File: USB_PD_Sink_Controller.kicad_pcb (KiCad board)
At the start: 2 copper layers, 43.5 x 30.5 mm, 24 parts, among them J1 USB_C_Receptacle_PowerOnly_6P, J2 Barrel_Jack, J3 Conn_01x15_Socket, J4 Conn_01x15_Socket, U1 STUSB4500QTR, U2 STL6P3LLH6, U3 STL6P3LLH6, U4 LM2931-5.0_SO8

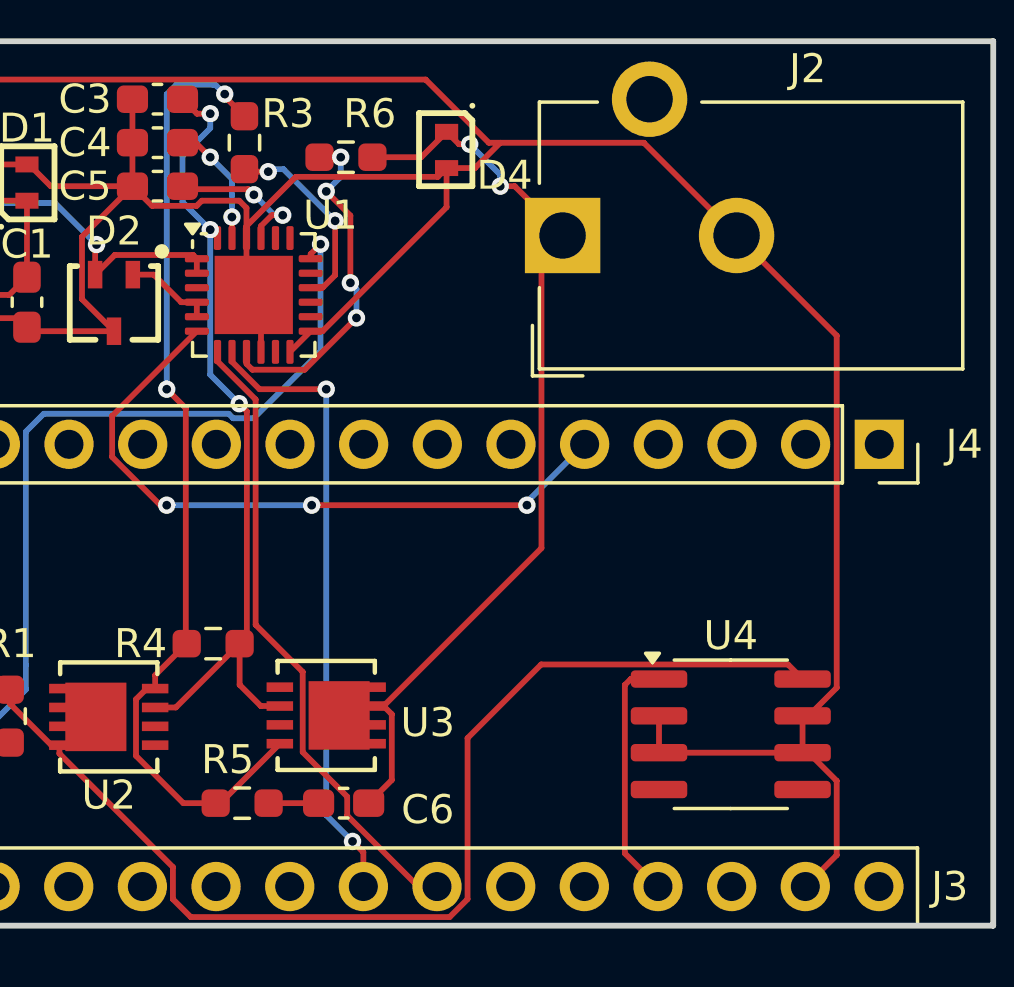
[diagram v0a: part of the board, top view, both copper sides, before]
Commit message: Added Pullup resistors and alert pin
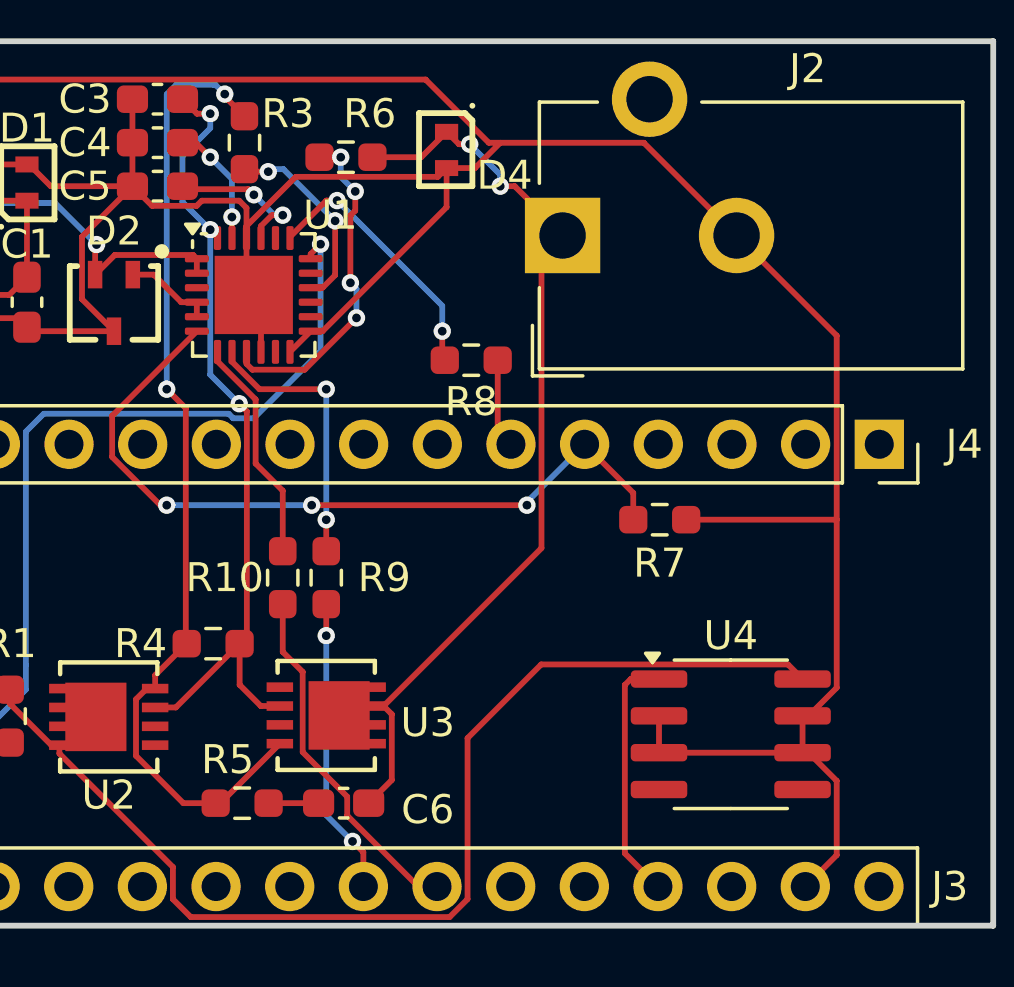
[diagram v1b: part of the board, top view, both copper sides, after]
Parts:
- added R10: 4.7kR, Resistor_SMD:R_0603_1608Metric_Pad0.98x0.95mm_HandSolder, F.Cu at (157.5, 95.5)
- added R7: 10kR, Resistor_SMD:R_0603_1608Metric_Pad0.98x0.95mm_HandSolder, F.Cu at (170.5, 93.5)
- added R8: 4.7kR, Resistor_SMD:R_0603_1608Metric_Pad0.98x0.95mm_HandSolder, F.Cu at (164.0, 88.0)
- added R9: 4.7kR, Resistor_SMD:R_0603_1608Metric_Pad0.98x0.95mm_HandSolder, F.Cu at (159.0, 95.5)
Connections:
- J4 pad 6: unconnected-(J4-Pin_6-Pad6) -> Net-(A1-D3)
- U1 pad 19: unconnected-(U1-ALERT-Pad19) -> Net-(U1-ALERT)
- U1 pad 7: Net-(A1-A5) -> Net-(U1-SCL)
- U1 pad 8: Net-(A1-A4) -> Net-(U1-SDA)
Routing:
- net Net-(A1-A4): track 21.7 -> 10.3 mm
- net Net-(A1-A5): track 22.0 -> 12.3 mm
- net Net-(U1-SDA): track 0.00 -> 9.57 mm, vias 0 -> 2
- net Net-(U1-ALERT): track 0.00 -> 9.22 mm, vias 0 -> 2
- net Net-(U1-SCL): track 0.00 -> 7.81 mm
- net GND: track 139.6 -> 144.8 mm
- net Net-(A1-D2): track 23.5 -> 26.8 mm
- net Net-(A1-D3): track 0.00 -> 3.09 mm

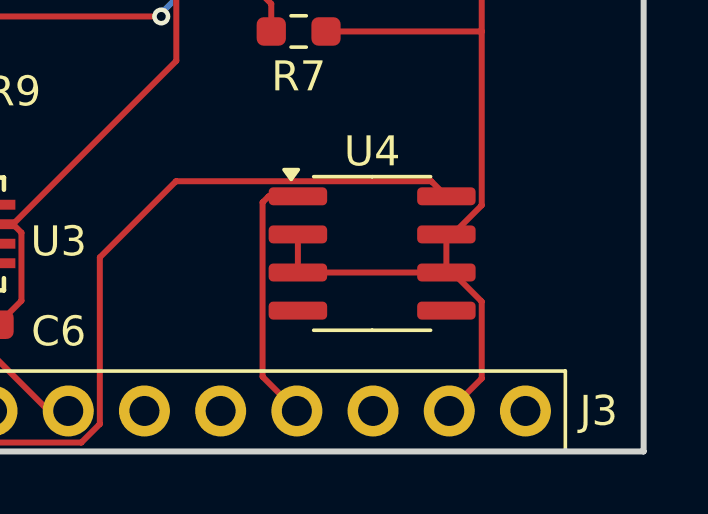
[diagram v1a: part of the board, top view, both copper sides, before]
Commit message: Added capacitor to linear voltage regulator
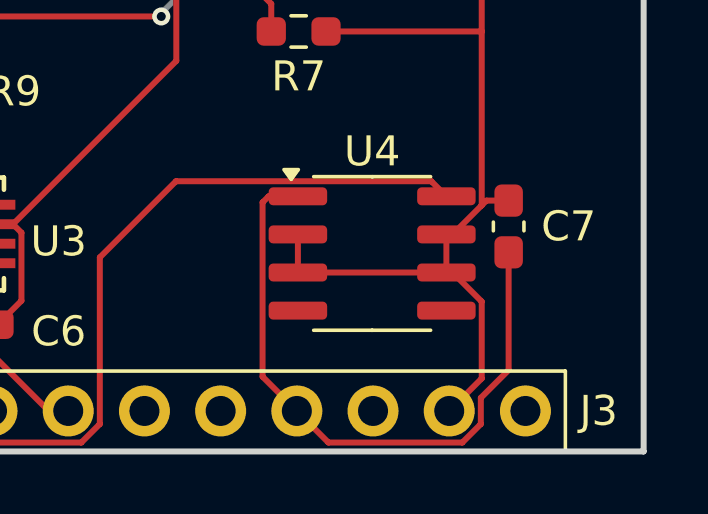
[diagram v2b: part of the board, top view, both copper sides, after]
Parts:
- added C7: 100μF, Capacitor_SMD:C_0603_1608Metric_Pad1.08x0.95mm_HandSolder, F.Cu at (177.5, 100.0)
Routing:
- net Net-(A1-+5V): track 8.69 -> 21.6 mm
- net GND: track 144.8 -> 145.7 mm
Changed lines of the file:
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@@
 		)
 	)
+	(footprint "Capacitor_SMD:C_0603_1608Metric_Pad1.08x0.95mm_HandSolder"
+		(layer "F.Cu")
+		(at 177.5 100 -90)
+		(descr "Capacitor SMD 0603 (1608 Metric), square (rectangular) end terminal, IPC-7351 nominal with elongated pad for handsoldering. (Body size source: IPC-SM-782 page 76, https://www.pcb-3d.com/wordpress/wp-content/uploads/ipc-sm-782a_amendment_1_and_2.pdf), generated with kicad-footprint-generator")
+		(tags "capacitor handsolder")
+		(property "Reference" "C7"
+			(at 0 -2 180)
+			(layer "F.SilkS")
+			(effects
+				(font
+					(size 1 1)
+					(thickness 0.15)
+				)
+			)
+		)
+		(property "Value" "100μF"
+			(at 0 1.43 90)
+			(layer "F.Fab")
+			(effects
+				(font
+					(size 1 1)
+					(thickness 0.15)
+				)
+			)
+		)
+		(property "Datasheet" "~"
+			(at 0 0 90)
+			(layer "F.Fab")
+			(hide yes)
+			(effects
+				(font
+					(size 1.27 1.27)
+					(thickness 0.15)
+				)
+			)
+		)
+		(property "Description" "Unpolarized capacitor"
+			(at 0 0 90)
+			(layer "F.Fab")
+			(hide yes)
+			(effects
+				(font
+					(size 1.27 1.27)
+					(thickness 0.15)
+				)
+			)
+		)
+		(property ki_fp_filters "C_*")
+		(sheetname "/")
+		(sheetfile "USB_PD_Sink_Controller.kicad_sch")
+		(attr smd)
+		(fp_line
+			(start -0.146267 0.51)
+			(end 0.146267 0.51)
+			(stroke
+				(width 0.12)
+				(type solid)
+			)
+			(layer "F.SilkS")
+		)
+		(fp_line
+			(start -0.146267 -0.51)
+			(end 0.146267 -0.51)
+			(stroke
+				(width 0.12)
+				(type solid)
+			)
+			(layer "F.SilkS")
+		)
+		(fp_line
+			(start -1.65 0.73)
+			(end -1.65 -0.73)
+			(stroke
+				(width 0.05)
+				(type solid)
+			)
+			(layer "F.CrtYd")
+		)
+		(fp_line
+			(start 1.65 0.73)
+			(end -1.65 0.73)
+			(stroke
+				(width 0.05)
+				(type solid)
+			)
+			(layer "F.CrtYd")
+		)
+		(fp_line
+			(start -1.65 -0.73)
+			(end 1.65 -0.73)
+			(stroke
+				(width 0.05)
+				(type solid)
+			)
+			(layer "F.CrtYd")
+		)
+		(fp_line
+			(start 1.65 -0.73)
+			(end 1.65 0.73)
+			(stroke
+				(width 0.05)
+				(type solid)
+			)
+			(layer "F.CrtYd")
+		)
+		(fp_line
+			(start -0.8 0.4)
+			(end -0.8 -0.4)
+			(stroke
+				(width 0.1)
+				(type solid)
+			)
+			(layer "F.Fab")
+		)
+		(fp_line
+			(start 0.8 0.4)
+			(end -0.8 0.4)
+			(stroke
+				(width 0.1)
+				(type solid)
+			)
+			(layer "F.Fab")
+		)
+		(fp_line
+			(start -0.8 -0.4)
+			(end 0.8 -0.4)
+			(stroke
+				(width 0.1)
+				(type solid)
+			)
+			(layer "F.Fab")
+		)
+		(fp_line
+			(start 0.8 -0.4)
+			(end 0.8 0.4)
+			(stroke
+				(width 0.1)
+				(type solid)
+			)
+			(layer "F.Fab")
+		)
+		(fp_text user "${REFERENCE}"
+			(at 0 0 90)
+			(layer "F.Fab")
+			(effects
+				(font
+					(size 0.4 0.4)
+					(thickness 0.06)
+				)
+			)
+		)
+		(pad "1" smd roundrect
+			(at -0.8625 0 270)
+			(size 1.075 0.95)
+			(layers "F.Cu" "F.Mask" "F.Paste")
+			(roundrect_rratio 0.25)
+			(net 2 "GND")
+			(pintype "passive")
+		)
+		(pad "2" smd roundrect
+			(at 0.8625 0 270)
+			(size 1.075 0.95)
+			(layers "F.Cu" "F.Mask" "F.Paste")
+			(roundrect_rratio 0.25)
+			(net 1 "Net-(A1-+5V)")
+			(pintype "passive")
+		)
+		(embedded_fonts no)
+		(model "${KICAD9_3DMODEL_DIR}/Capacitor_SMD.3dshapes/C_0603_1608Metric.step"
+			(offset
+				(xyz 0 0 0)
+			)
+			(scale
+				(xyz 1 1 1)
+			)
+			(rotate
+				(xyz 0 0 0)
+			)
+		)
+	)
 	(footprint "ST_1610:ST_1610"
 		(layer "F.Cu")
@@
 	)
 	(segment
+		(start 176.5726 105.713998)
+		(end 176.5726 106.586002)
+		(width 0.2)
+		(layer "F.Cu")
+		(net 1)
+	)
+	(segment
+		(start 176.5726 106.586002)
+		(end 175.956002 107.2026)
+		(width 0.2)
+		(layer "F.Cu")
+		(net 1)
+	)
+	(segment
 		(start 170.44 106.15)
 		(end 169.2974 105.0074)
@@
 	)
 	(segment
+		(start 177.5 104.786598)
+		(end 176.5726 105.713998)
+		(width 0.2)
+		(layer "F.Cu")
+		(net 1)
+	)
+	(segment
 		(start 169.2974 105.0074)
 		(end 169.2974 99.197601)
@@
 	)
 	(segment
+		(start 177.5 100.8625)
+		(end 177.5 104.786598)
+		(width 0.2)
+		(layer "F.Cu")
+		(net 1)
+	)
+	(segment
 		(start 169.500001 98.995)
 		(end 170.475 98.995)
@@
 	)
 	(segment
+		(start 171.4926 107.2026)
+		(end 170.44 106.15)
+		(width 0.2)
+		(layer "F.Cu")
+		(net 1)
+	)
+	(segment
+		(start 175.956002 107.2026)
+		(end 171.4926 107.2026)
+		(width 0.2)
+		(layer "F.Cu")
+		(net 1)
+	)
+	(segment
 		(start 150.5774 83.7401)
 		(end 152.3175 82)
@@
 	)
 	(segment
+		(start 176.76031 99.1375)
+		(end 176.6026 99.29521)
+		(width 0.2)
+		(layer "F.Cu")
+		(net 2)
+	)
+	(segment
 		(start 175.63281 101.535)
 		(end 176.6026 102.50479)
@@
 		(width 0.2)
 		(layer "F.Cu")
+		(net 2)
+	)
+	(segment
+		(start 177.5 99.1375)
+		(end 176.76031 99.1375)
+		(width 0.2)
+		(layer "F.Cu")

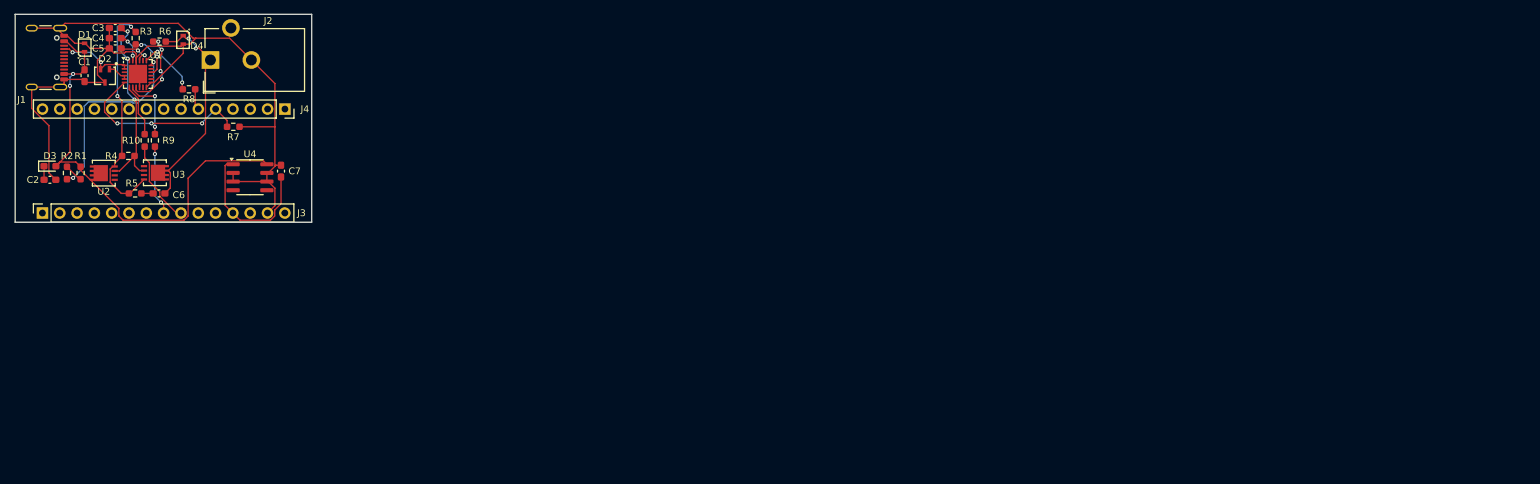
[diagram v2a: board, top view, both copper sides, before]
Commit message: Revamped the PCB design
Made many of the traces thicker. Changed from a barrel jack to a JST connector. Made the schematic pretty. Made the Arduino Nano directly soldered onto the board. Etc.
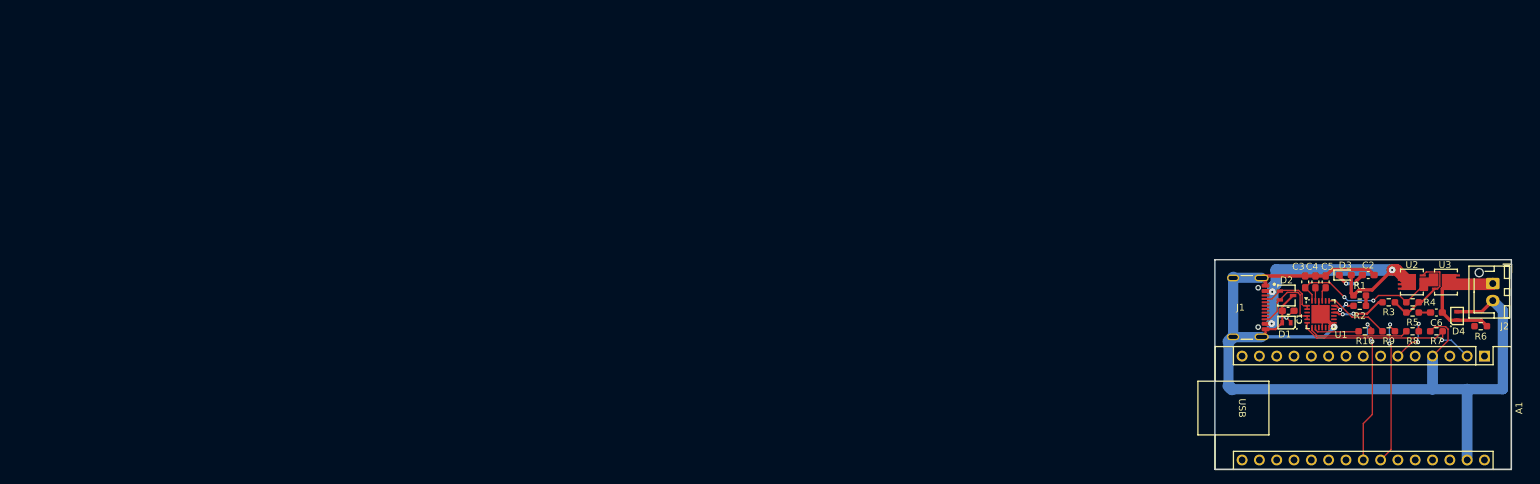
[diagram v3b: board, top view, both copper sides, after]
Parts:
- removed C7: 100μF, Capacitor_SMD:C_0603_1608Metric_Pad1.08x0.95mm_HandSolder
- removed J3, J4: Conn_01x15_Socket, Connector_PinSocket_2.54mm:PinSocket_1x15_P2.54mm_Vertical
- removed U4: LM2931-5.0_SO8, Package_SO:SOIC-8_3.9x4.9mm_P1.27mm
- added A1: Arduino_Nano_v2.x, Module:Arduino_Nano, F.Cu at (354.1, 127.1)
- J2: value Barrel_Jack -> JST_01x02_Socket; footprint Connector_BarrelJack:BarrelJack_CUI_PJ-102AH_Horizontal -> Connector_JST:JST_XH_B2B-XH-AM_1x02_P2.50mm_Vertical
- U2, U3: footprint STL6P3LLH6:POWERFLAT_3P3X3P3_STM -> STL6P3LLH6:POWERFLAT_3P3X3P3_STM2
- moved R6 198.3 mm to (353.5, 122.8)
- moved C2 193.9 mm to (337.0, 115.2)
- moved U2 192.6 mm to (343.4, 116.3)
- moved D4 191.2 mm to (350.0, 121.2), turned to 90 degrees
- moved J2 191.0 mm to (355.3, 116.5), turned to -90 degrees
- moved D3 190.7 mm to (333.6, 115.2)
- moved R2 190.6 mm to (335.8, 119.8), turned to 180 degrees
- moved U3 190.1 mm to (348.4, 116.3)
- moved R4 189.6 mm to (343.5, 119.2), turned to 180 degrees
- moved R1 188.5 mm to (335.8, 118.2), turned to 0 degrees
- moved C6 188.2 mm to (347.0, 120.8)
- moved R5 188.2 mm to (343.5, 120.8)
- moved R3 187.9 mm to (340.0, 119.2), turned to 180 degrees
- moved R9 183.2 mm to (340.0, 123.5), turned to 180 degrees
- moved R8 183.0 mm to (343.5, 123.5)
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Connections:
- net Net-(A1-D2) renamed /RESET
- net Net-(U1-DISCH) renamed /DISCH
- net Net-(U1-VBUS_EN_SNK) renamed /VBUS_EN_SNK
- net Net-(U1-VBUS_VS_DISCH) renamed /VBUS_VS_DISCH
- C1 pad 1: Net-(D1-K) -> /Vbus
- C3 pad 2: Net-(U1-VDD) -> /VDD
- D1 pad 1: Net-(D1-K) -> /Vbus
- D2 pad 1: Net-(J1-CC2) -> /CC1
- D2 pad 2: Net-(J1-CC1) -> /CC2
- D3 pad 2: Net-(D1-K) -> /Vbus
- J1 pad A5: Net-(J1-CC1) -> /CC1
- J1 pad A9: Net-(D1-K) -> /Vbus
- J1 pad B5: Net-(J1-CC2) -> /CC2
- J1 pad B9: Net-(D1-K) -> /Vbus
- R1 pad 1: Net-(D1-K) -> /Vbus
- R10 pad 2: Net-(U1-SCL) -> /SDA
- R4 pad 2: Net-(U1-VDD) -> /VDD
- R8 pad 2: Net-(U1-ALERT) -> /ALERT
- R9 pad 2: Net-(U1-SDA) -> /SCL
- U1 pad 1: Net-(J1-CC1) -> /CC1
- U1 pad 19: Net-(U1-ALERT) -> /SCL
- U1 pad 2: Net-(J1-CC1) -> /CC1
- U1 pad 24: Net-(U1-VDD) -> /VDD
- U1 pad 4: Net-(J1-CC2) -> /CC2
- U1 pad 5: Net-(J1-CC2) -> /CC2
- U1 pad 7: Net-(U1-SCL) -> /ALERT
- U1 pad 8: Net-(U1-SDA) -> /SDA
- U2 pad 1: unconnected-(U2-S-Pad1) -> Net-(U2-G)
- U2 pad 2: unconnected-(U2-S-Pad2) -> /VDD
- U2 pad 3: Net-(U1-VDD) -> /Vbus
- U3 pad 1: unconnected-(U3-S-Pad1) -> Net-(U2-G)
- U3 pad 2: Net-(U1-VDD) -> /VDD
- U3 pad 3: unconnected-(U3-S-Pad3) -> Net-(D4-K)
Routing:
- net Net-(D1-K): track 67.0 -> 0.00 mm, vias 2 -> 0
- net /Vbus: track 0.00 -> 45.2 mm, vias 0 -> 4
- net Net-(U1-VDD): track 28.2 -> 0.00 mm, vias 3 -> 0
- net /VBUS_VS_DISCH: track 28.0 -> 3.65 mm
- net /VDD: track 0.00 -> 22.5 mm, vias 0 -> 2
- net Net-(A1-+5V): track 21.6 -> 0.00 mm
- net Net-(U2-G): track 33.8 -> 13.6 mm, vias 2 -> 0
- net /ALERT: track 0.00 -> 14.9 mm
- net Net-(D4-K): track 31.2 -> 18.9 mm, vias 2 -> 0
- net /CC2: track 0.00 -> 12.3 mm
- net Net-(A1-A5): track 10.3 -> 22.0 mm
- net /DISCH: track 11.7 -> 0.00 mm, vias 4 -> 0
- net Net-(J1-CC1): track 11.6 -> 0.00 mm, vias 2 -> 0
- net /SCL: track 0.00 -> 9.69 mm
- net Net-(A1-A4): track 12.3 -> 21.9 mm, vias 0 -> 2
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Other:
- board size 43.5 x 30.5 mm -> 43.5 x 30.8 mm
